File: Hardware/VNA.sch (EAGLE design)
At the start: 316 parts, among them IC1 LTC5510, IC10 LT5560, IC11 LTC6362, IC12 MCP33131D-10-E/MS, IC13 SI5351C, IC14 MAX2871, IC15 NCP702-3.3, IC16 RFSW6042, IC17 AP2114H, IC18 RFSW6042, IC19 MAX2871, IC2 LT5560, IC20 NCP702-3.3, IC21 AP2114H, IC22 F2912, IC23 F1958, IC24 TRF37A73, IC25 F2912, IC26 F2912, IC27 F2912, IC3 LTC6362, IC4 MCP33131D-10-E/MS, IC5 LTC5510, IC6 LT5560, IC7 LTC6362, IC8 MCP33131D-10-E/MS, IC9 LTC5510, J1 U.FL-R-SMT, J2 U.FL-R-SMT, Q1 FA-128 26MHz, T1 MABA011082, T2 MABA011082, T3 MABA011082, X1 RLB DUT/RF IN, X2 RLB DUT/RF IN

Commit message: Placing
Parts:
- removed C106, C113: 100n, rcl:C-EUC0603
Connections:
- removed net N$100: C112.1, IC13.CLK4, L37.1
- new net N$160: C112.1, IC13.CLK5, L37.1
- net GND: no longer C106.1, C113.1
- net LO1_REF: now also IC13.CLK2; no longer IC13.CLK1
- net N$101: now also IC13.CLK4; no longer IC13.CLK2
- net N$109: no longer C106.2, C113.2
- net N$157: now also IC13.CLK0; no longer IC13.CLK5
- net N$23: now also T2.PIN2; no longer T2.PIN1
- net N$25: now also T2.PIN1; no longer T2.PIN2
- net N$97: now also IC13.CLK1; no longer IC13.CLK3
- net SOURCE_REF: now also IC13.CLK3; no longer IC13.CLK0

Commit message: Partial routing
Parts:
- removed R14, R26, R42: 51k, rcl:R-EU_R0603
- added C106, C158, C160, C162, C164, C165, C166, C167, C168, C193, C194, C195: 1u, rcl:C-EUC0603
- added C113, C159, C161, C163: 4u7, rcl:C-EUC0603
- added C169, C170, C171, C172, C174, C180, C181, C184, C189, C190: 22u, rcl:C-EUC1206
- added C173, C177, C185: 10u/25V, rcl:C-EUC1206
- added C175, C178, C186: 47n, rcl:C-EUC0603
- added C176: 510p, rcl:C-EUC0603
- added C179, C183: DNP, rcl:C-EUC0603
- added C182: 120p, rcl:C-EUC0603
- added C187: 1n, rcl:C-EUC0603
- added C188: 8p2, rcl:C-EUC0603
- added C191, C192, C203, C204, C205, C206, C207, C208, C209, C210, C211: 100n, rcl:C-EUC0603
- added IC28, IC29, IC30, IC31: LDL212PU50R, custom-ic:LDL212PU50R
- added IC32: TPS65265, custom-ic:TPS65265
- added IC33: STM32L432KC, custom-ic:STM32L432KC
- added IC34, IC35, IC36: NCP702-1.8, rf:NCP702
- added J3: DCJ0202, con-jack:DCJ0202
- added JP1: (no value), pinhead:PINHD-1X6
- added JTAG: (no value), con-ml:ML10
- added L47, L48, L49, L50: Ferrite, rf:INDUCTOR0603
- added L51, L55: 10u, custom-ic:SRN5040
- added L52, L53, L54: 6u8, custom-ic:SRN5040
- added R100, R101, R102, R103, R104, R90, R92, R93, R94, R95, R97, R98, R99: 10k, resistor:R-EU_R0603
- added R76, R88, R91, R96: 22, resistor:R-EU_R0603
- added R77: DNP, rcl:R-EU_R0603
- added R78: 51k, rcl:R-EU_R0603
- added R79: 82k, rcl:R-EU_R0603
- added R80, R83, R86: 10k, rcl:R-EU_R0603
- added R81: 91k, rcl:R-EU_R0603
- added R82: 30k, rcl:R-EU_R0603
- added R84: 45k3, rcl:R-EU_R0603
- added R85: 16k, rcl:R-EU_R0603
- added R87: 20k, rcl:R-EU_R0603
- added R89: 1k5, resistor:R-EU_R0603
- added U2: 6SLX9TQG144, xilinx_devices_V6:6SLX9TQG144
- added U4: W25Q16BVSN, memory-winbond:W25Q16BVSN
- added X3: MINI-USB-32005-201, con-cypressindustries:MINI-USB-32005-201
- C28, C63, C95: value 100n -> 1u; device resistor:C-EUC0603 -> rcl:C-EUC0603
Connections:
- removed net ADC_SCLK: IC12.SCLK, IC4.SCLK, IC8.SCLK
- removed net CONVSTART: IC12.CONVST, IC4.CONVST, IC8.CONVST
- removed net PORT1TEMP: IC1.TEMP, R14.2
- removed net PORT2TEMP: IC5.TEMP, R26.2
- removed net REFTEMP: IC9.TEMP, R42.2
- new net +12V: C173.1, C177.1, C185.1, IC32G1.VIN, IC32G2.VIN, IC32G3.VIN, J3.1
- new net FILT_IN_C1: R100.2, U2B3.IO_L42N_GCLK24_3
- new net FILT_IN_C2: R99.2, U2B3.IO_L44N_GCLK20_3
- new net FILT_OUT_C1: R104.2, U2B3.IO_L43N_GCLK22_IRDY2_3
- new net FILT_OUT_C2: R103.2, U2B3.IO_L44P_GCLK21_3
- new net FLACH_MOSI: U2B2.IO_L3N_MOSI_CSI_B_MISO0_2, U4.DI
- new net FLASH_CLK: U2B2.IO_L1P_CCLK_2, U4.CLK
- new net FLASH_CS: U2B2.IO_L65N_CSO_B_2, U4.!CS!
- new net FLASH_MISO: R91.1, U4.DO
- new net MCU_AUX1: IC33.PC14-OSC32_IN, U2B2.IO_L30N_GCLK0_USERCCLK_2
- new net MCU_AUX2: IC33.PC15-OSC32_OUT, U2B2.IO_L31P_GCLK31_D14_2
- new net MCU_AUX3: IC33.PA0/CK_IN/TIM2_CH1, U2B2.IO_L31N_GCLK30_D15_2
- new net MCU_AUX4: IC33.PA1/TIM2_CH2/SPI1_SCK, U2B2.IO_L48P_D7_2
- new net MCU_INTR: IC33.PB7/I2C1_SDA/USART1_RX, U2B2.IO_L14N_D12_2
- new net MCU_MISO: IC33.PB4/I2C3_SDA/SPI1_MISO/SPI3_MISO, U2B2.IO_L12N_D2_MISO3_2
- new net MCU_MOSI: IC33.PB5/SPI1_MOSI/SPI3_MOSI, U2B2.IO_L13N_D10_2
- new net MCU_NSS: IC33.PB6/I2C1_SCL/USART1_TX, U2B2.IO_L14P_D11_2
- new net MCU_SCK: IC33.PB3/TIM2_CH2/SPI1_SCK/SPI3_SCK, U2B2.IO_L30P_GCLK1_D13_2
- new net N$100: C113.2, IC28.SENSE, IC28.VOUT, L47.1
- new net N$161: C159.2, IC29.SENSE, IC29.VOUT, L48.1
- new net N$162: C168.2, IC32COMMON.V7V
- new net N$163: C106.2, C158.2, C160.2, C162.2, C174.1, C181.1, IC28.EN, IC28.VIN, IC29.EN, IC29.VIN, IC30.EN, IC30.VIN, IC31.EN, IC31.VIN, L51.2
- new net N$164: C161.2, IC30.SENSE, IC30.VOUT, L49.1
- new net N$165: JTAG.3, U2BNA.TDO
- new net N$166: C163.2, IC31.SENSE, IC31.VOUT, L50.1
- new net N$167: IC32COMMON.PSM, R77.2
- new net N$168: C178.2, IC32G1.BST
- new net N$169: C178.1, IC32G1.LX, L52.1
- new net N$170: C175.2, IC32G2.BST
- new net N$171: C175.1, IC32G2.LX, L53.1
- new net N$172: C176.2, IC32G2.COMP, R82.2
- new net N$173: JTAG.5, U2BNA.TMS
- new net N$174: C182.2, IC32G1.COMP, R79.2
- new net N$175: JTAG.9, U2BNA.TDI
- new net N$176: C183.2, IC32G1.FB, R80.2, R81.1
- new net N$177: C170.1, C171.1, C183.1, L51.1, L52.2, R81.2
- new net N$178: C179.2, IC32G2.FB, R83.2, R84.1
- new net N$179: C169.1, C172.1, C179.1, L53.2, L55.1, R84.2
- new net N$180: C186.2, IC32G3.BST
- new net N$181: C186.1, IC32G3.LX, L54.1
- new net N$182: C187.2, IC32G3.COMP, R85.2
- new net N$183: JTAG.1, U2BNA.TCK
- new net N$184: C188.2, IC32G3.FB, R86.2, R87.1
- new net N$185: R88.1, X3.2
- new net N$186: R76.2, R89.2, X3.3
- new net N$187: IC33.PA11/TIM1_CH4/SPI1_MISO/CAN1_RX/USB_DM, R88.2
- new net N$188: IC33.PA12/SPI1_MOSI/CAN1_TX/USB_DP, R76.1
- new net N$189: IC33.PA15/TIM2_CH1/USART2_RX/SPI1_NSS/SPI3_NSS, R89.1
- new net N$190: IC33.PA14/SWCLK, JP1.2
- new net N$191: IC33.PA13/SWDIO, JP1.4
- new net N$192: IC33.NRST, JP1.5
- new net N$193: IC33.PA2/TIM2_CH3/USART2_TX, JP1.6
- new net N$194: R92.1, U2B2.DONE_2
- new net N$195: R93.1, U2B2.IO_L65P_INIT_B_2
- new net N$196: R94.1, U2B2.PROGRAM_B_2
- new net N$197: R91.2, U2B2.IO_L3P_D0_DIN_MISO_MISO1_2
- new net N$198: R96.2, U2B3.IO_L43P_GCLK23_3
- new net N$199: IC16.C1, R97.1, R99.1
- new net N$200: IC16.C2, R100.1, R98.1
- new net N$201: IC18.C2, R101.1, R103.1
- new net N$202: IC18.C1, R102.1, R104.1
- new net N$203: C194.1, IC34.VOUT, IC4.AVDD
- new net N$204: C63.1, IC35.VOUT, IC8.AVDD
- new net N$205: C195.1, IC12.AVDD, IC36.VOUT
- new net PORT1_CONVSTART: IC4.CONVST, U2B0.IO_L34P_GCLK19_0
- new net PORT1_SCLK: IC4.SCLK, U2B0.IO_L35P_GCLK17_0
- new net PORT2_CONVSTART: IC8.CONVST, U2B2.IO_L48N_RDWR_B_VREF_2
- new net PORT2_SCLK: IC8.SCLK, U2B2.IO_L49N_D4_2
- new net REF_CONVSTART: IC12.CONVST, U2B2.IO_L62N_D6_2
- new net REF_SCLK: IC12.SCLK, U2B2.IO_L64N_D9_2
- new net SWITCHING_SYNC: IC32COMMON.ROSC, R78.2, U2B2.IO_L12P_D1_MISO2_2
- new net VCCINT: C180.1, C184.1, C188.1, C208.1, C209.1, C210.1, C211.1, L54.2, R87.2, U2BVCCINT.VCCINT@0, U2BVCCINT.VCCINT@1, U2BVCCINT.VCCINT@2, U2BVCCINT.VCCINT@3, U2BVCCINT.VCCINT@4
- net +3V3: now also C189.1, C190.1, C191.1, C192.1, C203.1, C204.1, C205.1, C206.1, C207.1, IC33.VDD1, IC33.VDD2, IC33.VDDA/VREF+, JP1.1, JTAG.4, L55.2, R90.2, R92.2, R93.2, R94.2, R95.2, U2B0.VCCO_0@0, U2B0.VCCO_0@1, U2B0.VCCO_0@2, U2B1.VCCO_1@0, U2B1.VCCO_1@1, U2B1.VCCO_1@2, U2B2.IO_L1N_M0_CMPMISO_2, U2B2.VCCO_2@0, U2B2.VCCO_2@1, U2B3.VCCO_3@0, U2B3.VCCO_3@1, U2B3.VCCO_3@2, U2BVCCAUX.VCCAUX@0, U2BVCCAUX.VCCAUX@1, U2BVCCAUX.VCCAUX@2, U2BVCCAUX.VCCAUX@3, U2BVCCAUX.VCCAUX@4, U4.!HOLD!, U4.!WP!, U4.VCC
- net +5V/1: now also C164.2, C193.1, IC34.EN, IC34.VIN, L47.2; no longer C28.2, IC4.AVDD, R14.1
- net +5V/2: now also C165.2, C28.1, IC35.EN, IC35.VIN, L48.2; no longer C63.2, IC8.AVDD, R26.1
- net +5V/3: now also C166.2, C95.1, IC36.EN, IC36.VIN, L49.2; no longer C95.2, IC12.AVDD, R42.1
- net +5V/4: now also C167.2, L50.2
- net AMP_PWDN: now also U2B3.IO_L41P_GCLK27_3
- net ATT_D0: now also U2B3.IO_L37N_3
- net ATT_D1: now also U2B3.IO_L37P_3
- net ATT_D2: now also U2B3.IO_L36N_3
- net ATT_D3: now also U2B3.IO_L36P_3
- net ATT_D4: now also U2B3.IO_L2N_3
- net ATT_D5: now also U2B3.IO_L2P_3
- net ATT_D6: now also U2B3.IO_L1N_VREF_3
- net BAND_SELECT: now also U2B3.IO_L42P_GCLK25_TRDY2_3
- net FPGA_CLK: now also R96.1
- net GND: now also C106.1, C113.1, C158.1, C159.1, C160.1, C161.1, C162.1, C163.1, C164.1, C165.1, C166.1, C167.1, C168.1, C169.2, C170.2, C171.2, C172.2, C173.2, C174.2, C176.1, C177.2, C180.2, C181.2, C182.1, C184.2, C185.2, C187.1, C189.2, C190.2, C191.2, C192.2, C193.2, C194.2, C195.2, C203.2, C204.2, C205.2, C206.2, C207.2, C208.2, C209.2, C210.2, C211.2, C28.2, C63.2, C95.2, IC28.GND, IC29.GND, IC30.GND, IC31.GND, IC32COMMON.AGND, IC32G1.GND, IC32G2.GND, IC32G3.GND, IC33.BOOT0, IC33.EP, IC33.VSS1, IC33.VSS2, IC34.GND, IC35.GND, IC36.GND, J3.3, JP1.3, JTAG.10, JTAG.2, R101.2, R102.2, R77.1, R78.1, R79.1, R80.1, R82.1, R83.1, R85.1, R86.1, R97.2, R98.2, U2B2.IO_L13P_M1_2, U2BGND.GND@0, U2BGND.GND@1, U2BGND.GND@10, U2BGND.GND@11, U2BGND.GND@12, U2BGND.GND@2, U2BGND.GND@3, U2BGND.GND@4, U2BGND.GND@5, U2BGND.GND@6, U2BGND.GND@7, U2BGND.GND@8, U2BGND.GND@9, U2BNA.SUSPEND, U4.GND, X3.5; no longer C28.1, C63.1, C95.1
- net LO1_CE: now also U2B3.IO_L52P_3
- net LO1_CLK: now also U2B3.IO_L50N_3
- net LO1_EN: now also U2B3.IO_L49N_3
- net LO1_LD: now also U2B3.IO_L49P_3
- net LO1_LE: now also U2B3.IO_L51N_3
- net LO1_MOSI: now also U2B3.IO_L51P_3
- net LO1_MUX: now also U2B3.IO_L50P_3
- net N$122: now also LP1.IN; no longer LP1.OUT
- net N$123: now also LP1.OUT; no longer LP1.IN
- net N$124: now also LP3.OUT; no longer LP3.IN
- net N$125: now also LP2.OUT; no longer LP2.IN
- net N$126: now also LP2.IN; no longer LP2.OUT
- net N$127: now also LP3.IN; no longer LP3.OUT
- net PORT1MIX_EN: now also U2B0.IO_L4N_0
- net PORT1_SDO: now also U2B0.IO_L34N_GCLK18_0
- net PORT2MIX_EN: now also U2B2.IO_L62P_D5_2
- net PORT2_SDO: now also U2B2.IO_L49P_D3_2
- net PORT_SELECT: now also U2B3.IO_L41N_GCLK26_3
- net REFMIX_EN: now also U2B3.IO_L1P_3
- net REF_SDO: now also U2B2.IO_L64P_D8_2
- net SCL: now also IC33.PA9/TIM1_CH2/I2C1_SCL/USART1_TX, R90.1
- net SDA: now also IC33.PA10/TIM1_CH3/I2C1_SDA/USART1_RX, R95.1
- net SOURCE_CE: now also U2B3.IO_L52N_3
- net SOURCE_CLK: now also U2B0.IO_L1P_HSWAPEN_0
- net SOURCE_LD: now also U2B0.IO_L2N_0
- net SOURCE_LE: now also U2B3.IO_L83P_3
- net SOURCE_MOSI: now also U2B3.IO_L83N_VREF_3
- net SOURCE_MUX: now also U2B0.IO_L1N_VREF_0
- net SOURCE_RF_EN: now also U2B0.IO_L2P_0
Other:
- note added: "FPGA + MCU Connections"
- note added: "Port 1 Mixers, up to 200mA"
- note added: "Port 2 Mixers, up to 200mA"
- note added: "Reference Mixers, up to 200mA"
- note added: "Resistor set for 1MHz, can be overwritten by signal at ROSC"
- note added: "Source and 1.LO, up to 350mA"
- note added: "Up to 100mA"
- note added: "Up to 60mA on 3V3"

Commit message: Routing
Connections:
- removed net LO1_EN: IC19.RFOUT_EN, U2B3.IO_L49N_3
- new net LO1_RF_EN: IC19.RFOUT_EN, U2B0.IO_L1N_VREF_0
- net ATT_D0: now also U2B3.IO_L1N_VREF_3; no longer U2B3.IO_L37N_3
- net ATT_D1: now also U2B3.IO_L2P_3; no longer U2B3.IO_L37P_3
- net ATT_D2: now also U2B3.IO_L2N_3; no longer U2B3.IO_L36N_3
- net ATT_D4: now also U2B3.IO_L36N_3; no longer U2B3.IO_L2N_3
- net ATT_D5: now also U2B3.IO_L37P_3; no longer U2B3.IO_L2P_3
- net ATT_D6: now also U2B3.IO_L37N_3; no longer U2B3.IO_L1N_VREF_3
- net FILT_IN_C1: now also U2B3.IO_L43N_GCLK22_IRDY2_3; no longer U2B3.IO_L42N_GCLK24_3
- net FILT_IN_C2: now also U2B3.IO_L44P_GCLK21_3; no longer U2B3.IO_L44N_GCLK20_3
- net FILT_OUT_C1: now also U2B3.IO_L42N_GCLK24_3; no longer U2B3.IO_L43N_GCLK22_IRDY2_3
- net FILT_OUT_C2: now also U2B3.IO_L43P_GCLK23_3; no longer U2B3.IO_L44P_GCLK21_3
- net LO1_CE: now also U2B0.IO_L4P_0; no longer U2B3.IO_L52P_3
- net LO1_CLK: now also U2B0.IO_L2N_0; no longer U2B3.IO_L50N_3
- net LO1_LD: now also U2B0.IO_L2P_0; no longer U2B3.IO_L49P_3
- net LO1_LE: now also U2B0.IO_L3N_0; no longer U2B3.IO_L51N_3
- net LO1_MOSI: now also U2B0.IO_L3P_0; no longer U2B3.IO_L51P_3
- net LO1_MUX: now also U2B0.IO_L1P_HSWAPEN_0; no longer U2B3.IO_L50P_3
- net N$198: now also U2B3.IO_L44N_GCLK20_3; no longer U2B3.IO_L43P_GCLK23_3
- net SCL: now also U2B3.IO_L52P_3
- net SDA: now also U2B3.IO_L50N_3
- net SOURCE_CE: now also U2B3.IO_L83N_VREF_3; no longer U2B3.IO_L52N_3
- net SOURCE_CLK: now also U2B3.IO_L51N_3; no longer U2B0.IO_L1P_HSWAPEN_0
- net SOURCE_LD: now also U2B3.IO_L50P_3; no longer U2B0.IO_L2N_0
- net SOURCE_MOSI: now also U2B3.IO_L52N_3; no longer U2B3.IO_L83N_VREF_3
- net SOURCE_MUX: now also U2B3.IO_L51P_3; no longer U2B0.IO_L1N_VREF_0
- net SOURCE_RF_EN: now also U2B3.IO_L49N_3; no longer U2B0.IO_L2P_0
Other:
- moved on the sheet: R96

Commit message: Routing
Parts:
- removed X3: MINI-USB-32005-201, con-cypressindustries:MINI-USB-32005-201
- added X4: MINI-USB-SCHIELD-32005-301, con-cypressindustries:MINI-USB-SCHIELD-32005-301
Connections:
- net GND: now also X4G$1.5, X4S.S1, X4S.S2, X4S.S3, X4S.S4; no longer X3.5
- net N$185: now also X4G$1.2; no longer X3.2
- net N$186: now also X4G$1.3; no longer X3.3
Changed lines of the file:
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@@
 <part name="GND212" library="supply1" deviceset="GND" device=""/>
 <part name="SUPPLY29" library="supply2" deviceset="+12V" device=""/>
-<part name="X3" library="con-cypressindustries" deviceset="MINI-USB-" device="32005-201"/>
 <part name="U2" library="xilinx_devices_V6" deviceset="6SLX9TQG144" device=""/>
 <part name="JTAG" library="con-ml" deviceset="ML10" device=""/>
@@
 <part name="SUPPLY21" library="supply2" deviceset="+5V/3" device=""/>
 <part name="SUPPLY14" library="supply2" deviceset="+5V/2" device=""/>
+<part name="X4" library="con-cypressindustries" deviceset="MINI-USB-SCHIELD-" device="32005-301"/>
 </parts>
 <sheets>
@@
 </plain>
 <instances>
-<instance part="X3" gate="G$1" x="223.52" y="66.04" smashed="yes">
-<attribute name="NAME" x="220.98" y="77.47" size="1.778" layer="95"/>
-<attribute name="VALUE" x="233.68" y="58.42" size="1.778" layer="96" rot="R90"/>
-</instance>
 <instance part="U2" gate="B2" x="327.66" y="190.5" smashed="yes" rot="MR0">
 <attribute name="NAME" x="327.66" y="231.902" size="1.778" layer="95"/>
@@
 <attribute name="VALUE" x="76.2" y="66.04" size="1.778" layer="96"/>
 </instance>
-<instance part="GND217" gate="1" x="215.9" y="55.88" smashed="yes">
-<attribute name="VALUE" x="213.36" y="53.34" size="1.778" layer="96"/>
+<instance part="GND217" gate="1" x="215.9" y="45.72" smashed="yes">
+<attribute name="VALUE" x="213.36" y="43.18" size="1.778" layer="96"/>
 </instance>
 <instance part="R76" gate="G$1" x="203.2" y="66.04" smashed="yes">
@@
 <attribute name="VALUE" x="50.8" y="81.28" size="1.778" layer="96"/>
 </instance>
+<instance part="X4" gate="G$1" x="223.52" y="66.04" smashed="yes">
+<attribute name="NAME" x="220.98" y="77.47" size="1.778" layer="95"/>
+<attribute name="VALUE" x="233.68" y="58.42" size="1.778" layer="96" rot="R90"/>
+</instance>
+<instance part="X4" gate="S" x="223.52" y="55.88" smashed="yes">
+<attribute name="NAME" x="231.14" y="53.34" size="1.778" layer="95"/>
+</instance>
 </instances>
 <busses>
@@
 </segment>
 <segment>
-<pinref part="X3" gate="G$1" pin="5"/>
 <pinref part="GND217" gate="1" pin="GND"/>
 <wire x1="218.44" y1="60.96" x2="215.9" y2="60.96" width="0.1524" layer="91"/>
-<wire x1="215.9" y1="60.96" x2="215.9" y2="58.42" width="0.1524" layer="91"/>
+<wire x1="215.9" y1="60.96" x2="215.9" y2="50.8" width="0.1524" layer="91"/>
+<pinref part="X4" gate="G$1" pin="5"/>
+<pinref part="X4" gate="S" pin="S4"/>
+<wire x1="215.9" y1="50.8" x2="215.9" y2="48.26" width="0.1524" layer="91"/>
+<wire x1="215.9" y1="50.8" x2="220.98" y2="50.8" width="0.1524" layer="91"/>
+<wire x1="220.98" y1="50.8" x2="223.52" y2="50.8" width="0.1524" layer="91"/>
+<wire x1="223.52" y1="50.8" x2="226.06" y2="50.8" width="0.1524" layer="91"/>
+<wire x1="226.06" y1="50.8" x2="228.6" y2="50.8" width="0.1524" layer="91"/>
+<wire x1="228.6" y1="50.8" x2="228.6" y2="53.34" width="0.1524" layer="91"/>
+<junction x="215.9" y="50.8"/>
+<pinref part="X4" gate="S" pin="S3"/>
+<wire x1="226.06" y1="53.34" x2="226.06" y2="50.8" width="0.1524" layer="91"/>
+<junction x="226.06" y="50.8"/>
+<pinref part="X4" gate="S" pin="S2"/>
+<wire x1="223.52" y1="53.34" x2="223.52" y2="50.8" width="0.1524" layer="91"/>
+<junction x="223.52" y="50.8"/>
+<pinref part="X4" gate="S" pin="S1"/>
+<wire x1="220.98" y1="53.34" x2="220.98" y2="50.8" width="0.1524" layer="91"/>
+<junction x="220.98" y="50.8"/>
 </segment>
 <segment>
@@
 <net name="N$185" class="0">
 <segment>
-<pinref part="X3" gate="G$1" pin="2"/>
 <pinref part="R88" gate="G$1" pin="1"/>
 <wire x1="218.44" y1="68.58" x2="208.28" y2="68.58" width="0.1524" layer="91"/>
+<pinref part="X4" gate="G$1" pin="2"/>
 </segment>
 </net>
 <net name="N$186" class="0">
 <segment>
-<pinref part="X3" gate="G$1" pin="3"/>
 <pinref part="R76" gate="G$1" pin="2"/>
 <wire x1="218.44" y1="66.04" x2="213.36" y2="66.04" width="0.1524" layer="91"/>
@@
 <wire x1="213.36" y1="60.96" x2="213.36" y2="66.04" width="0.1524" layer="91"/>
 <junction x="213.36" y="66.04"/>
+<pinref part="X4" gate="G$1" pin="3"/>
 </segment>
 </net>

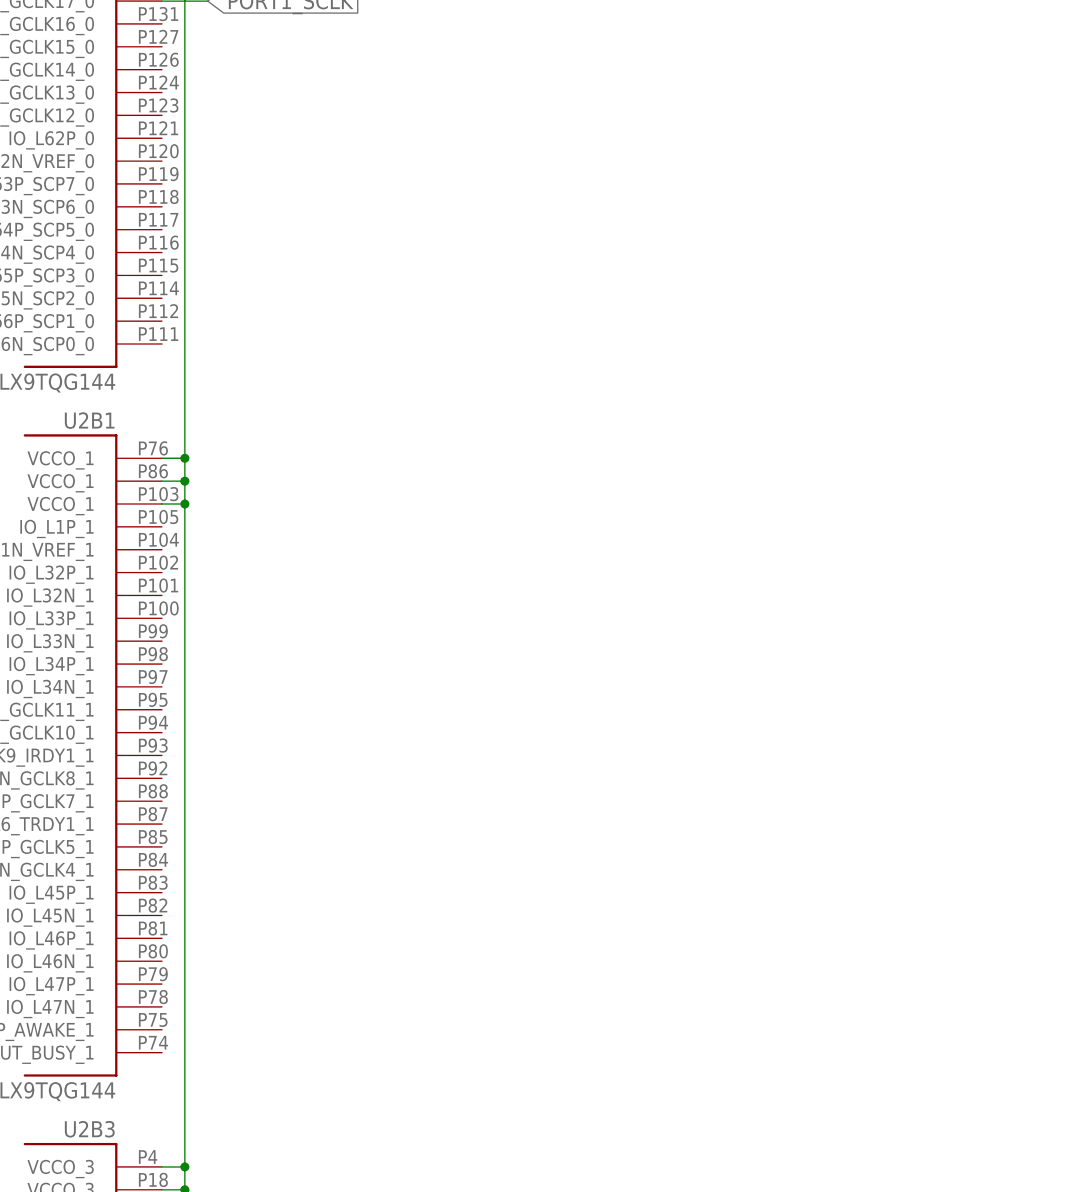
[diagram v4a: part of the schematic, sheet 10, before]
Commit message: Shield outline and small layout fixes
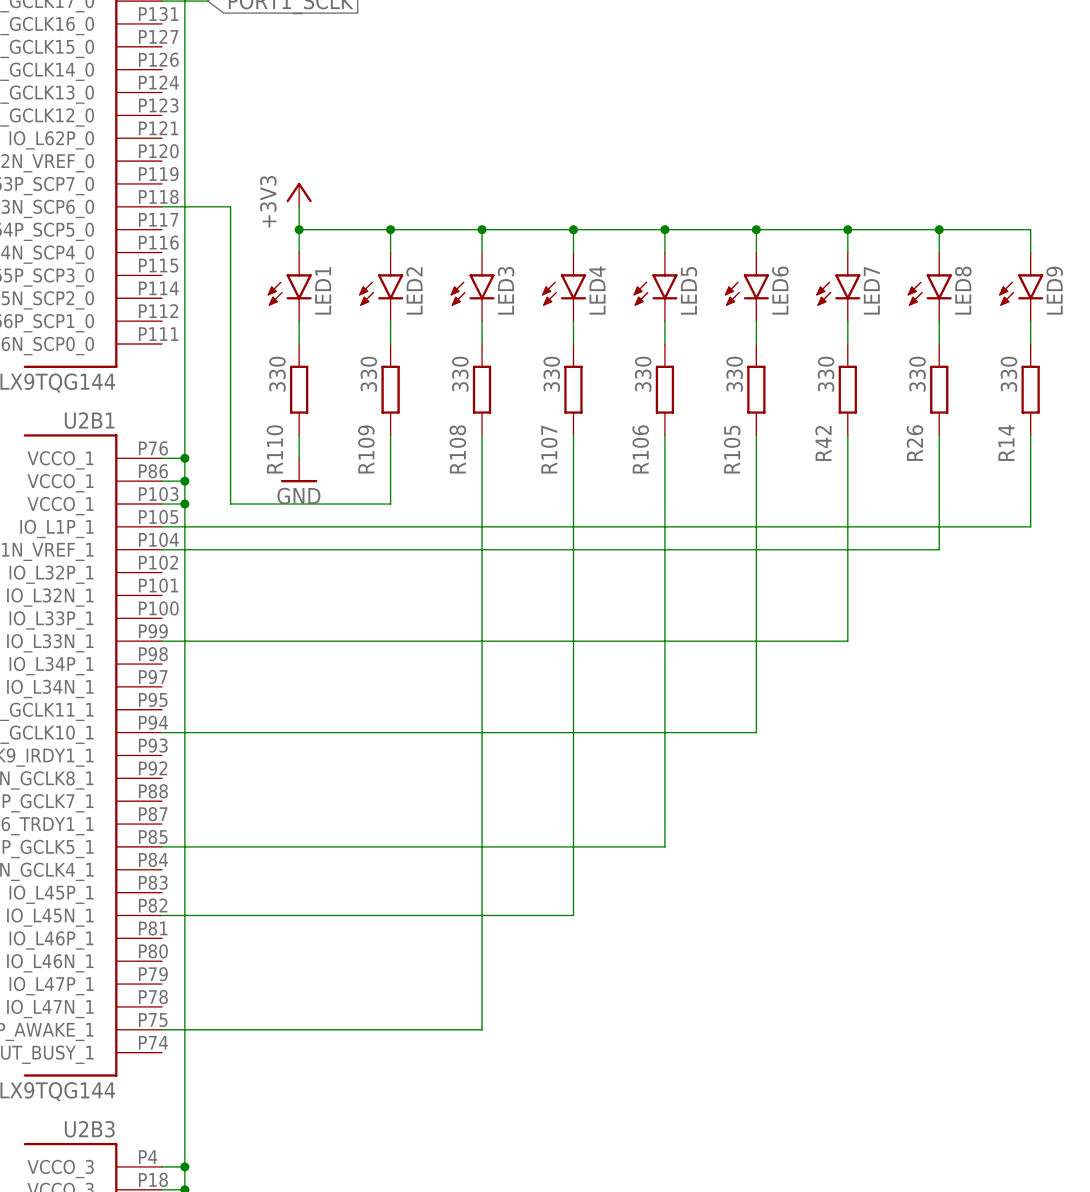
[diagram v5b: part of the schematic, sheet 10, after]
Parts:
- added LED1, LED2, LED3, LED4, LED5, LED6, LED7, LED8, LED9: (no value), led:LEDCHIPLED_0603
- added R105, R106, R107, R108, R109, R110, R14, R26, R42: 330, VNA:R-EU_R0603
- C1, C10, C104, C105, C106, C107, C108, C109, C11, C110, C113, C114, C115, C116, C117, C118, C119, C12, C120, C121, C122, C123, C124, C127, C128, C129, C13, C130, C131, C132, C133, C134, C135, C136, C137, C138, C139, C14, C140, C143, C144, C145, C146, C147, C148, C149, C150, C151, C152, C153, C154, C155, C156, C157, C158, C159, C160, C161, C162, C163, C164, C165, C166, C167, C168, C175, C176, C178, C179, C182, C183, C186, C187, C188, C191, C192, C193, C194, C195, C2, C203, C204, C205, C206, C207, C208, C209, C210, C211, C28, C3, C31, C32, C33, C34, C35, C36, C37, C38, C39, C4, C40, C41, C42, C43, C44, C5, C55, C56, C57, C58, C6, C63, C65, C66, C67, C68, C69, C7, C70, C71, C72, C73, C74, C75, C76, C8, C87, C88, C89, C9, C90, C95: device rcl:C-EUC0603 -> VNA:C-EUC0603
- C100, C101, C102, C103, C111, C112, C15, C16, C17, C18, C19, C20, C21, C22, C23, C24, C25, C26, C27, C29, C30, C45, C46, C47, C48, C49, C50, C51, C52, C53, C54, C59, C60, C61, C62, C64, C77, C78, C79, C80, C81, C82, C83, C84, C85, C86, C91, C92, C93, C94, C96, C97, C98, C99: device resistor:C-EUC0603 -> VNA:C-EUC0603
- C125, C126, C141, C142, C169, C170, C171, C172, C173, C174, C177, C180, C181, C184, C185, C189, C190: device rcl:C-EUC1206 -> VNA:C-EUC1206
- IC1, IC5, IC9: device rf:LTC5510 -> VNA:LTC5510
- IC10, IC2, IC6: device rf:LT5560 -> VNA:LT5560
- IC11, IC3, IC7: device rf:LTC6362 -> VNA:LTC6362
- IC12, IC4, IC8: device custom-ic:MCP33131D-10-E/MS -> VNA:MCP33131D-10-E/MS
- IC13: device rf:SI5351C -> VNA:SI5351C
- IC14, IC19: device rf:MAX2871 -> VNA:MAX2871
- IC15, IC20, IC34, IC35, IC36: device rf:NCP702 -> VNA:NCP702
- IC16, IC18: device rf:RFSW6042 -> VNA:RFSW6042
- IC17, IC21: device rf:AP2114H -> VNA:AP2114H
- IC22, IC25, IC26, IC27: device rf:F2912 -> VNA:F2912
- IC23: device rf:F1958 -> VNA:F1958
- IC24: device rf:TRF37A73 -> VNA:TRF37A73
- IC28, IC29, IC30, IC31: device custom-ic:LDL212PU50R -> VNA:LDL212PU50R
- IC32: device custom-ic:TPS65265 -> VNA:TPS65265
- IC33: device custom-ic:STM32L432KC -> VNA:STM32L432KC
- J1, J2: device connector:U.FL-R-SMT -> VNA:U.FL-R-SMT
- J3: device con-jack:DCJ0202 -> VNA:DCJ0202
- JP1: device pinhead:PINHD-1X6 -> VNA:PINHD-1X6
- JTAG: device con-ml:ML10 -> VNA:ML10
- L1, L10, L11, L12, L13, L14, L15, L16, L17, L18, L19, L2, L20, L21, L22, L23, L24, L25, L26, L27, L28, L29, L3, L30, L31, L32, L33, L34, L35, L36, L37, L38, L39, L4, L40, L41, L42, L43, L44, L45, L46, L47, L48, L49, L5, L50, L6, L7, L8, L9: device rf:INDUCTOR0603 -> VNA:INDUCTOR0603
- L51, L52, L53, L54, L55: device custom-ic:SRN5040 -> VNA:SRN5040
- LP1, LP2, LP3: device rf:LP0603A -> VNA:LP0603A
- Q1: device crystal:FA-128 -> VNA:FA-128
- R1, R10, R11, R12, R13, R15, R16, R17, R18, R19, R2, R20, R21, R22, R23, R24, R25, R27, R28, R29, R3, R30, R31, R32, R33, R34, R35, R36, R37, R38, R39, R4, R40, R41, R43, R44, R45, R46, R47, R48, R49, R5, R6, R7, R73, R74, R75, R77, R78, R79, R8, R80, R81, R82, R83, R84, R85, R86, R87, R9: device rcl:R-EU_R0603 -> VNA:R-EU_R0603
- R100, R101, R102, R103, R104, R50, R51, R52, R53, R54, R55, R56, R57, R58, R59, R60, R61, R62, R63, R64, R65, R66, R67, R68, R69, R70, R71, R72, R76, R88, R89, R90, R91, R92, R93, R94, R95, R96, R97, R98, R99: device resistor:R-EU_R0603 -> VNA:R-EU_R0603
- T1, T2, T3: device rf:MABA011082 -> VNA:MABA011082
- U2: device xilinx_devices_V6:6SLX9TQG144 -> VNA:6SLX9TQG144
- U4: device memory-winbond:W25Q16BVSN -> VNA:W25Q16BVSN
- X1, X2: device rf:SMA_CONNECTOR -> VNA:SMA_CONNECTOR
- X4: device con-cypressindustries:MINI-USB-SCHIELD-32005-301 -> VNA:MINI-USB-SCHIELD-32005-301
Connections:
- new net N$206: LED9.C, R14.1
- new net N$207: LED8.C, R26.1
- new net N$208: LED7.C, R42.1
- new net N$209: LED6.C, R105.1
- new net N$210: LED5.C, R106.1
- new net N$211: LED4.C, R107.1
- new net N$212: LED3.C, R108.1
- new net N$213: LED2.C, R109.1
- new net N$214: LED1.C, R110.1
- new net N$215: R14.2, U2B1.IO_L1P_1
- new net N$216: R26.2, U2B1.IO_L1N_VREF_1
- new net N$217: R42.2, U2B1.IO_L33N_1
- new net N$218: R105.2, U2B1.IO_L40N_GCLK10_1
- new net N$219: R106.2, U2B1.IO_L43P_GCLK5_1
- new net N$220: R107.2, U2B1.IO_L45N_1
- new net N$221: R108.2, U2B1.IO_L74P_AWAKE_1
- new net N$222: R109.2, U2B0.IO_L63N_SCP6_0
- net +3V3: now also LED1.A, LED2.A, LED3.A, LED4.A, LED5.A, LED6.A, LED7.A, LED8.A, LED9.A
- net GND: now also R110.2
